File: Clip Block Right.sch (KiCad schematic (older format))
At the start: 18 parts, among them SW17 B3F-5050, SW18 B3F-5050, SW19 B3F-5050, SW20 B3F-5050, SW21 B3F-5050, SW22 B3F-5050, SW23 B3F-5050, SW24 B3F-5050, SW25 B3F-5050, SW26 B3F-5050, SW27 B3F-5050, SW28 B3F-5050, SW29 B3F-5050, SW30 B3F-5050, SW31 B3F-5050, SW32 B3F-5050, U2 CD74HC4067M

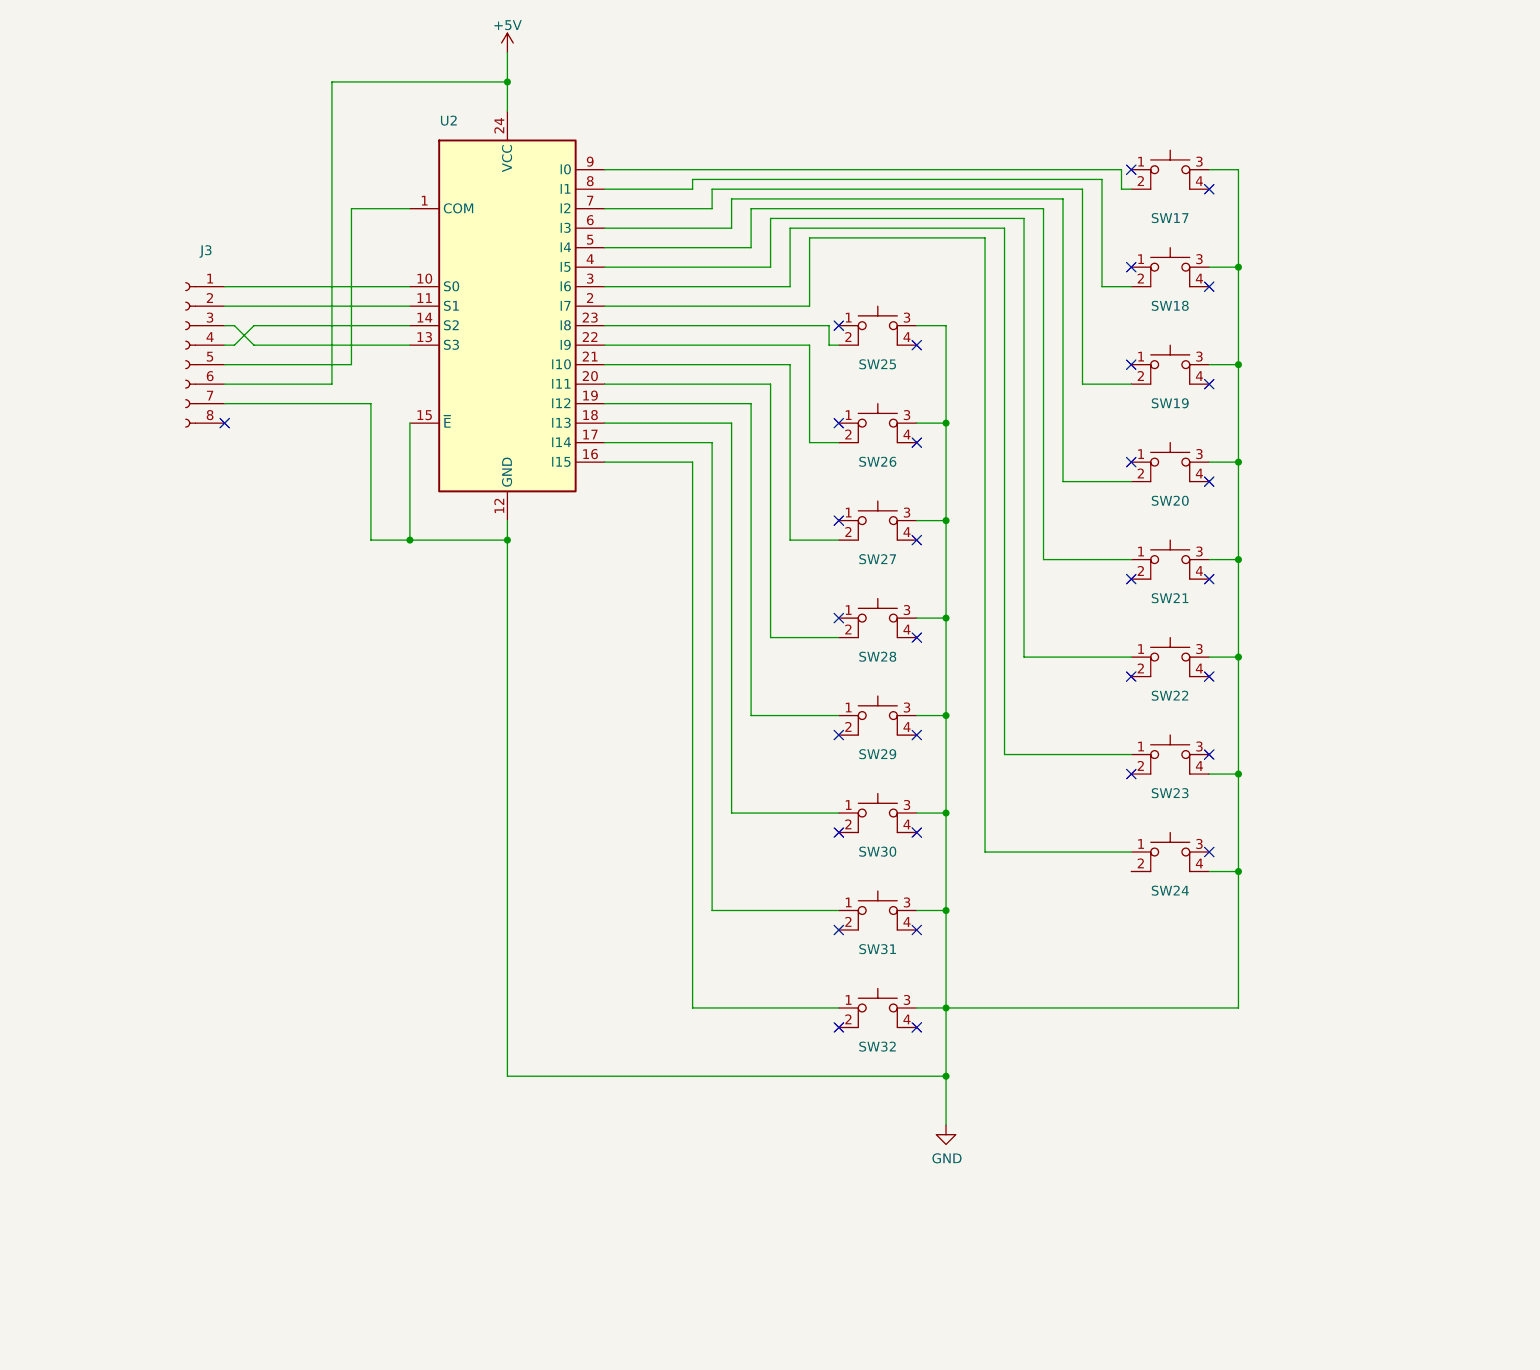
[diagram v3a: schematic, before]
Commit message: Redesign of upper boards
Added bussed resistors following Igor's correction to the schematic + tidied schematic.
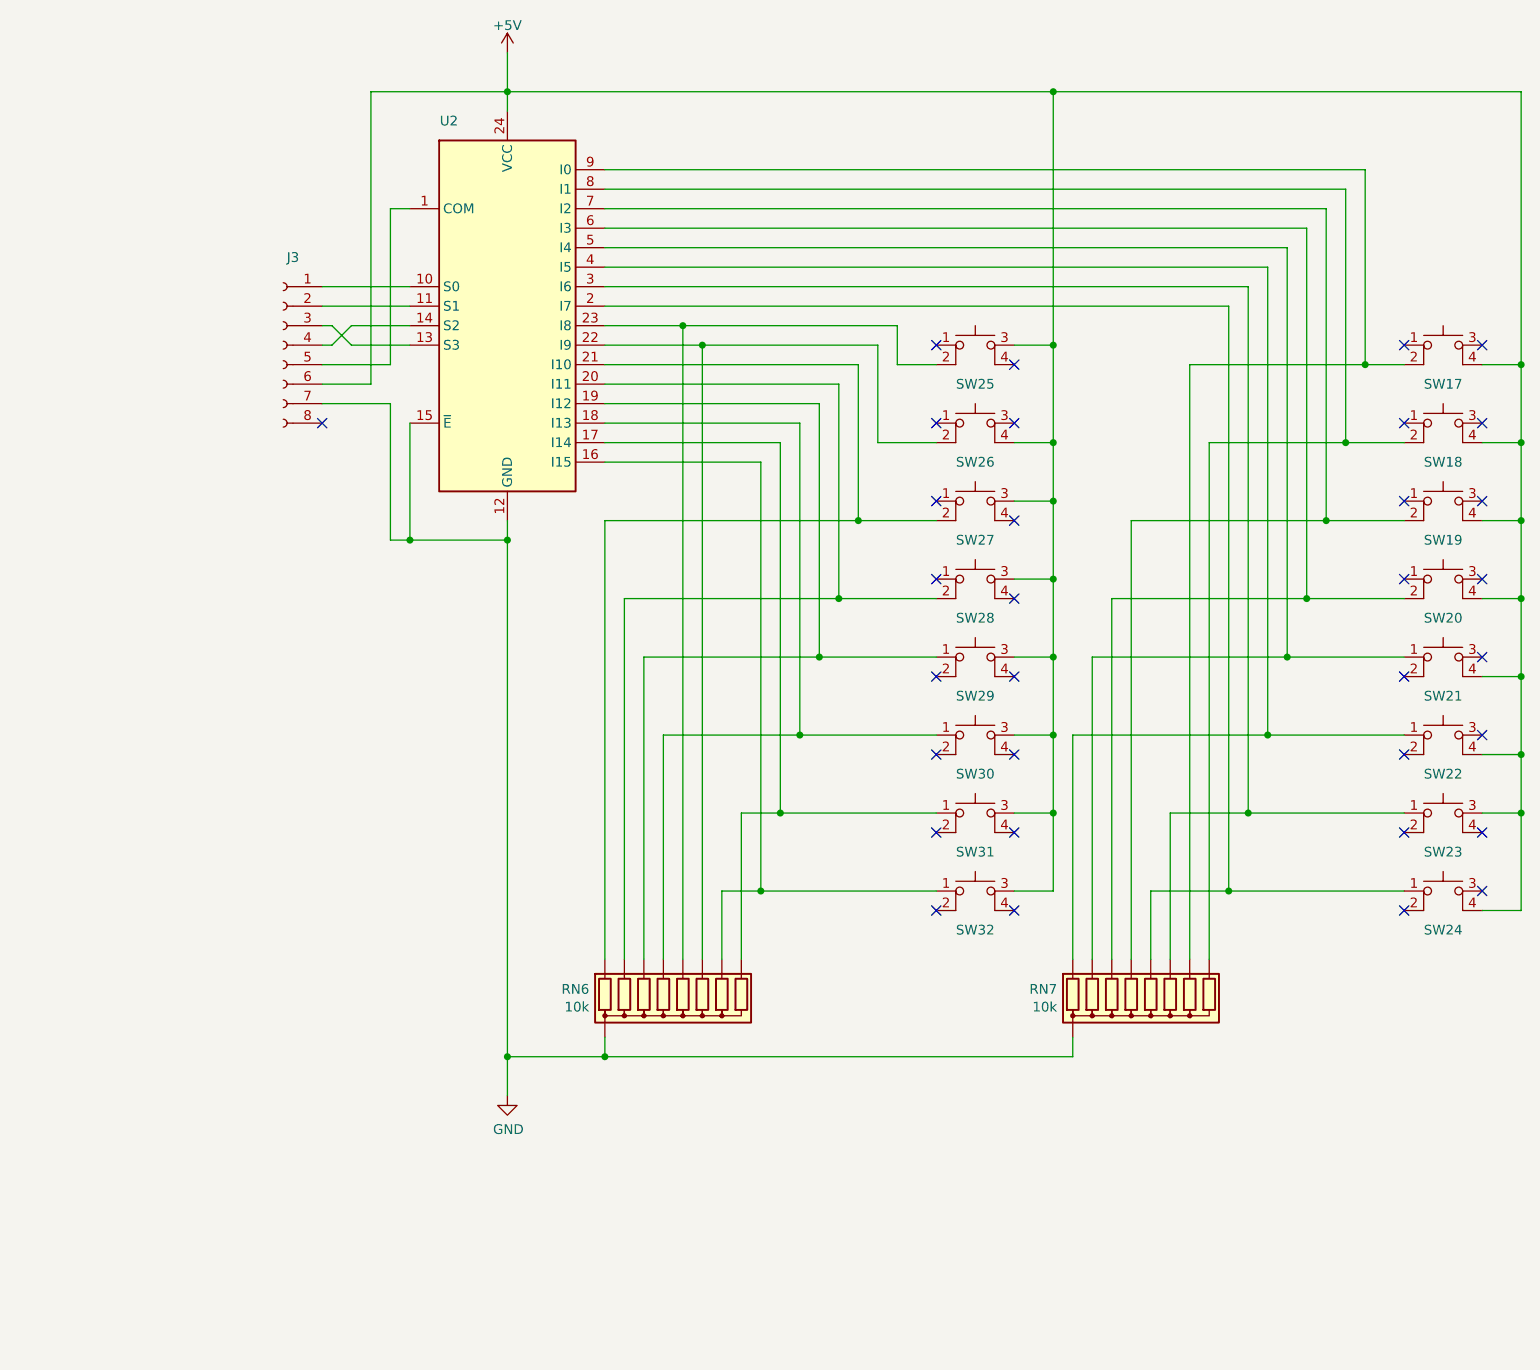
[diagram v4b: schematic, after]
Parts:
- added RN6, RN7: 10k, Resistor_THT:R_Array_SIP9, symbol Device:R_Network08
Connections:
- net +5V: now also SW17.4, SW18.4, SW19.4, SW20.4, SW21.4, SW22.4, SW23.3, SW24.4, SW25.3, SW26.4, SW27.3, SW28.3, SW29.3, SW30.3, SW31.3, SW32.3
- net GND: now also RN6.1 (common), RN7.1 (common); no longer SW17.3, SW18.3, SW19.3, SW20.3, SW21.3, SW22.3, SW23.4, SW24.4, SW25.3, SW26.3, SW27.3, SW28.3, SW29.3, SW30.3, SW31.3, SW32.3
- net at SW17.2, U2.9 (I0): now also RN7.8 (R7)
- net at SW18.2, U2.8 (I1): now also RN7.9 (R8)
- net at SW19.2, U2.7 (I2): now also RN7.5 (R4)
- net at SW20.2, U2.6 (I3): now also RN7.4 (R3)
- net at SW21.1 (A), U2.5 (I4): now also RN7.3 (R2)
- net at SW22.1 (A), U2.4 (I5): now also RN7.2 (R1)
- net at SW23.1 (A), U2.3 (I6): now also RN7.7 (R6)
- net at SW24.1 (A), U2.2 (I7): now also RN7.6 (R5)
- net at SW25.2, U2.23 (I8): now also RN6.6 (R5)
- net at SW26.2, U2.22 (I9): now also RN6.7 (R6)
- net at SW27.2, U2.21 (I10): now also RN6.2 (R1)
- net at SW28.2, U2.20 (I11): now also RN6.3 (R2)
- net at SW29.1 (A), U2.19 (I12): now also RN6.4 (R3)
- net at SW30.1 (A), U2.18 (I13): now also RN6.5 (R4)
- net at SW31.1 (A), U2.17 (I14): now also RN6.9 (R8)
- net at SW32.1 (A), U2.16 (I15): now also RN6.8 (R7)
- no-connect marks 32 -> 33
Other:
- moved on the sheet: J3, SW17, SW18, SW19, SW20, SW21, SW22, SW23, SW24, SW25, SW26, SW27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

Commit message: Resize boards and update connector
Resized the boards to fit the new modular height and started changing the interboard connectors
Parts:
- J3: footprint cunabulapress-footprints:Connector_TE_Connectivity_Micro-MaTch_8_Position_Female -> Connector_PinHeader_2.54mm:PinHeader_1x06_P2.54mm_Vertical; symbol Connector:Conn_01x08_Female -> Connector:Conn_01x06_Female
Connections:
- net GND: no longer J3.7 (Pin_7)
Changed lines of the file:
@@
-	1    0    0    -1
-$EndComp
-$Comp
-L 74xx:CD74HC4067M U?
-U 1 1 5C60BBCB
-P 2700 2250
-AR Path="/5C4B73B3/5C60BBCB" Ref="U?"  Part="1"
-AR Path="/5C4B9DB9/5C60BBCB" Ref="U2"  Part="1"
-F 0 "U2" H 2400 3200 50  0000 C CNN
-F 1 "CD74HC4067M" H 2700 3337 50  0001 C CNN
-F 2 "Package_SO:SOIC-24W_7.5x15.4mm_P1.27mm" H 3600 1250 50  0001 C CIN
-F 3 "http://www.ti.com/lit/ds/symlink/cd74hc4067.pdf" H 2350 3100 50  0001 C CNN
-	1    2700 2250
 	1    0    0    -1
 $EndComp
@@
 	2700 950  2700 1150
 $Comp
-L Connector:Conn_01x08_Female J?
+L Connector:Conn_01x06_Female J?
 U 1 1 5CE4BEBC
-P 1550 2450
+P 1550 2350
 AR Path="/5C3B66BD/5CE4BEBC" Ref="J?"  Part="1"
 AR Path="/5C4B9DB9/5CE4BEBC" Ref="J3"  Part="1"
-F 0 "J3" H 1500 2900 50  0000 C CNN
-F 1 "~" H 1444 2844 50  0000 C CNN
-F 2 "cunabulapress-footprints:Connector_TE_Connectivity_Micro-MaTch_8_Position_Female" H 1550 2450 50  0001 C CNN
-F 3 "~" H 1550 2450 50  0001 C CNN
-	1    1550 2450
+F 0 "J3" H 1500 2800 50  0000 C CNN
+F 1 "~" H 1444 2744 50  0000 C CNN
+F 2 "Connector_PinHeader_2.54mm:PinHeader_1x06_P2.54mm_Vertical" H 1550 2350 50  0001 C CNN
+F 3 "~" H 1550 2350 50  0001 C CNN
+	1    1550 2350
 	-1   0    0    -1
 $EndComp
@@
 Wire Wire Line
 	2000 1150 2000 2650
-Wire Wire Line
-	2100 2750 2100 3450
-Wire Wire Line
-	2100 3450 2200 3450
-Connection ~ 2200 3450
 $Comp
 L cp_midi_control_surface_002-rescue:SW_SPST_4_PIN-sw_spst_0 SW?
@@
 	1900 2450 1800 2350
 Wire Wire Line
-	1800 2350 1750 2350
-Wire Wire Line
-	1750 2450 1800 2450
-Wire Wire Line
 	1800 2450 1900 2350
 $Comp
@@
 	6400 5250 7300 5250
 Wire Wire Line
+	1900 2450 2200 2450
+Wire Wire Line
+	1900 2350 2200 2350
+Wire Wire Line
+	2100 1750 2200 1750
+Wire Wire Line
+	2000 1150 2700 1150
+Wire Wire Line
+	1750 2650 2000 2650
+Wire Wire Line
 	1750 2550 2100 2550
 Wire Wire Line
-	1750 2650 2000 2650
-Wire Wire Line
-	1750 2750 2100 2750
-Wire Wire Line
-	1900 2450 2200 2450
-Wire Wire Line
-	1900 2350 2200 2350
-Wire Wire Line
-	2200 2250 1750 2250
+	1750 2450 1800 2450
+Wire Wire Line
+	1750 2350 1800 2350
 Wire Wire Line
 	1750 2150 2200 2150
-Wire Wire Line
-	2100 1750 2200 1750
-Wire Wire Line
-	2000 1150 2700 1150
+$Comp
+L 74xx:CD74HC4067M U?
+U 1 1 5C60BBCB
+P 2700 2250
+AR Path="/5C4B73B3/5C60BBCB" Ref="U?"  Part="1"
+AR Path="/5C4B9DB9/5C60BBCB" Ref="U2"  Part="1"
+F 0 "U2" H 2400 3200 50  0000 C CNN
+F 1 "CD74HC4067M" H 2700 3337 50  0001 C CNN
+F 2 "Package_SO:SOIC-24W_7.5x15.4mm_P1.27mm" H 3600 1250 50  0001 C CIN
+F 3 "http://www.ti.com/lit/ds/symlink/cd74hc4067.pdf" H 2350 3100 50  0001 C CNN
+	1    2700 2250
+	1    0    0    -1
+$EndComp
+Wire Wire Line
+	1750 2250 2200 2250
 $EndSCHEMATC

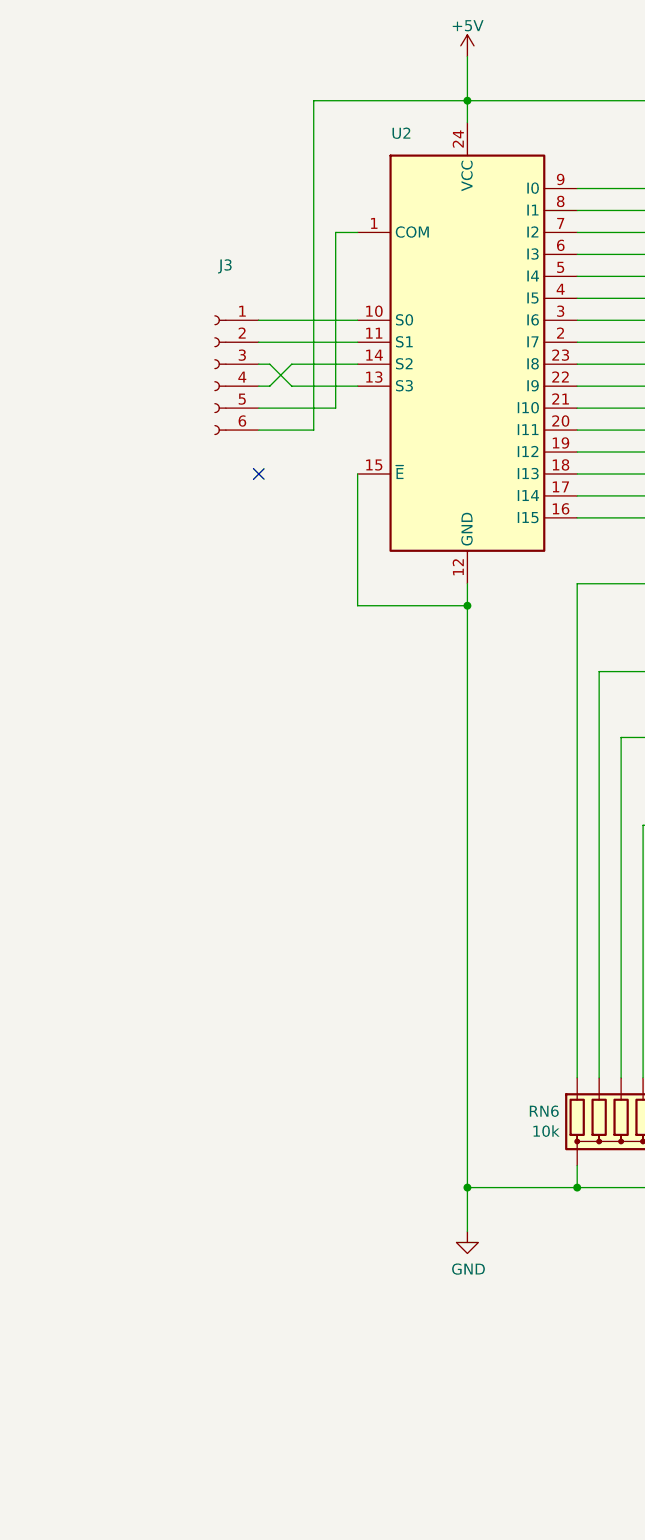
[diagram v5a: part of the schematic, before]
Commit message: Further cleanup and placement
Removed all the connectors to the rails as they're irrelevant to the top boards.

Added all the support headers.

Need to work out the correct routing for the headers but the placement is correct.
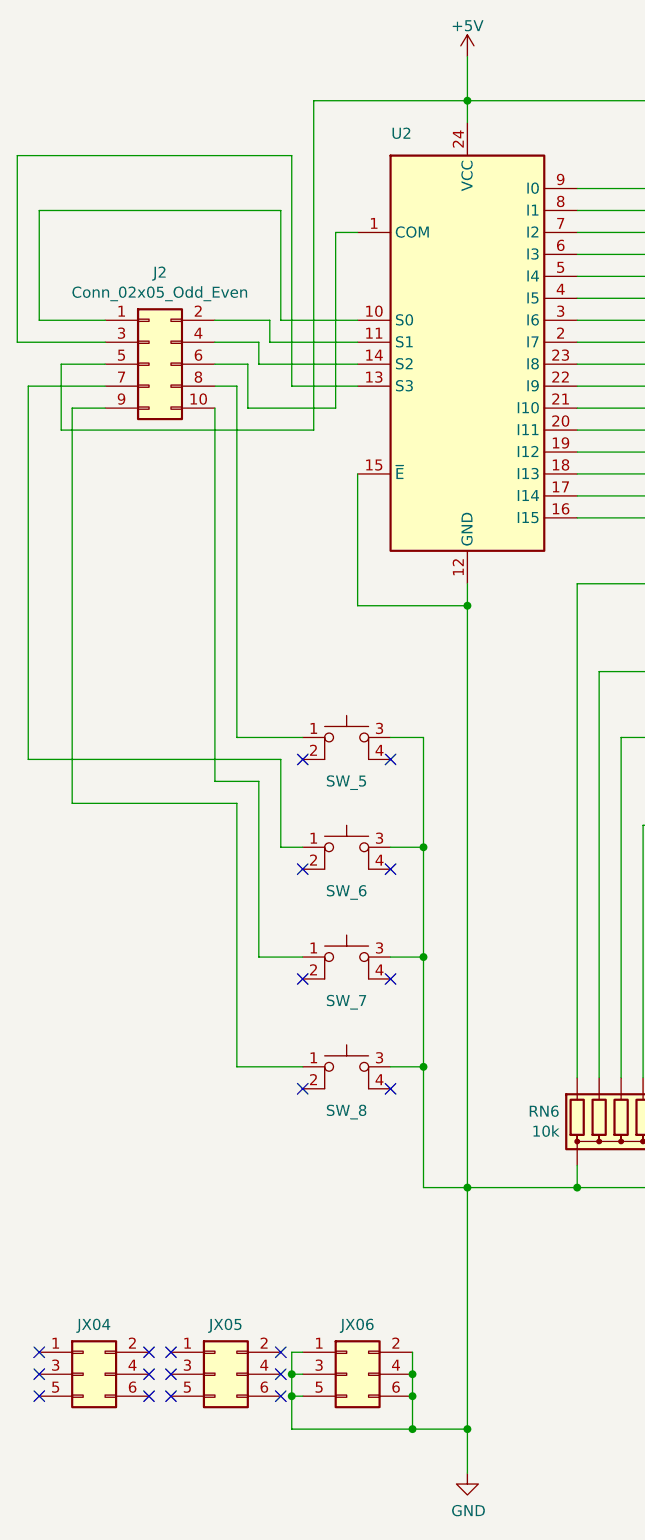
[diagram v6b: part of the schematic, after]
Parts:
- removed J3: ~, Connector_PinHeader_2.54mm:PinHeader_1x06_P2.54mm_Vertical, symbol Connector:Conn_01x06_Female
- added J2: Conn_02x05_Odd_Even, Connector_PinHeader_2.54mm:PinHeader_2x05_P2.54mm_Vertical, symbol Connector_Generic:Conn_02x05_Odd_Even
- added JX04, JX05, JX06: Conn_02x03_Odd_Even, Connector_PinHeader_2.54mm:PinHeader_2x03_P2.54mm_Vertical, symbol Connector_Generic:Conn_02x03_Odd_Even
- added SW_5, SW_6, SW_7, SW_8: B3F-5050, cunabulapress-footprints:Omron_B3F-5050, symbol cp_midi_control_surface_002-rescue:SW_SPST_4_PIN-sw_spst_0
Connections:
- net +5V: now also J2.5 (Pin_5)
- net GND: now also JX06.1 (Pin_1), JX06.2 (Pin_2), JX06.3 (Pin_3), JX06.4 (Pin_4), JX06.5 (Pin_5), JX06.6 (Pin_6), SW_5.3, SW_6.3, SW_7.3, SW_8.3
- net at U2.1 (COM): now also J2.6 (Pin_6)
- net at U2.10 (S0): now also J2.1 (Pin_1)
- net at U2.11 (S1): now also J2.2 (Pin_2)
- net at U2.13 (S3): now also J2.3 (Pin_3)
- net at U2.14 (S2): now also J2.4 (Pin_4)
- new net: J2.8 (Pin_8), SW_5.1 (A)
- new net: J2.7 (Pin_7), SW_6.1 (A)
- new net: J2.10 (Pin_10), SW_7.1 (A)
- new net: J2.9 (Pin_9), SW_8.1 (A)
- no-connect marks 33 -> 52
